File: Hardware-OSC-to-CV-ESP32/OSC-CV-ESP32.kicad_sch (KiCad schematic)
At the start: 10 parts, among them U1 MCP4822, U2 LM324, U3 ESP32-S3-DevKitC, U4 MCP4822

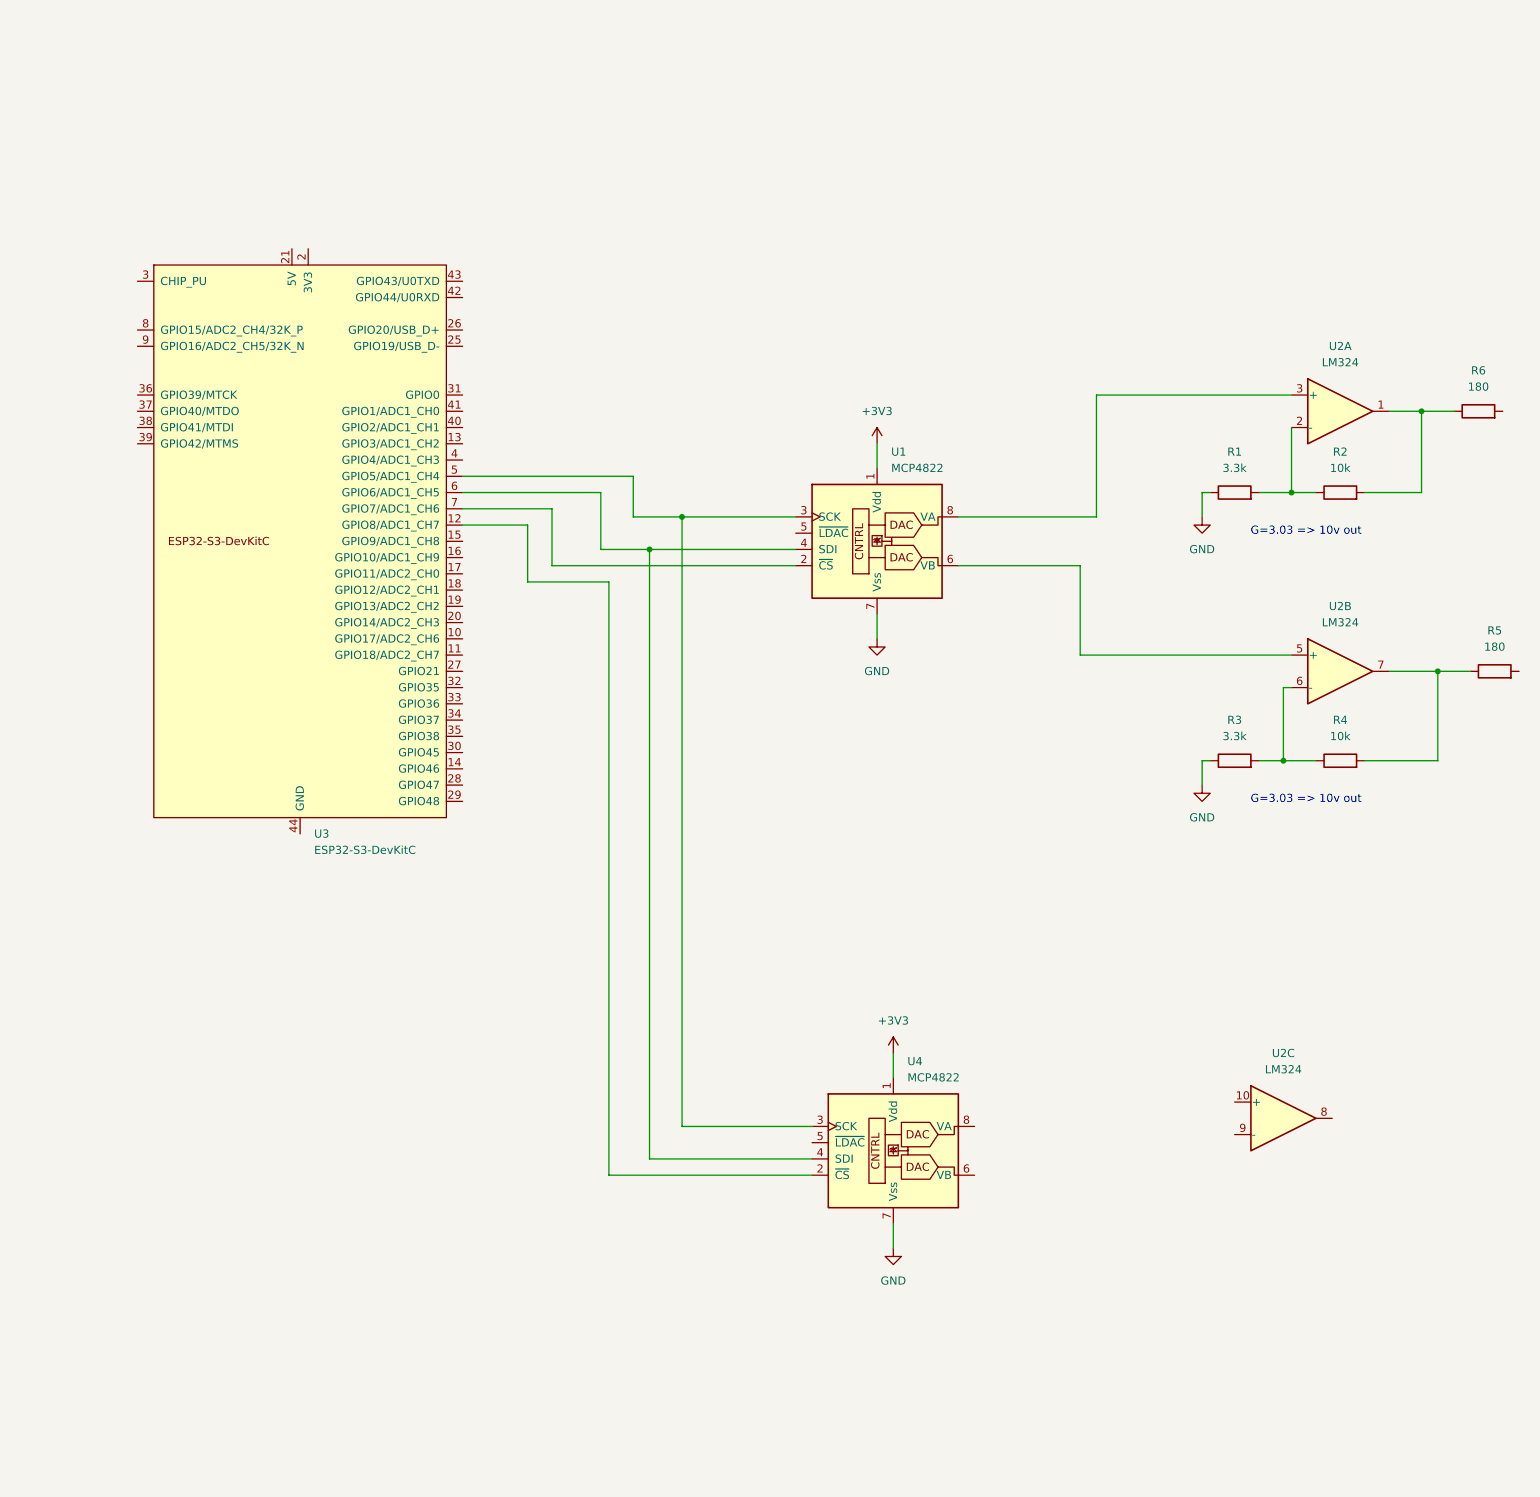
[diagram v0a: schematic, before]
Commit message: update schematic + 3D holder
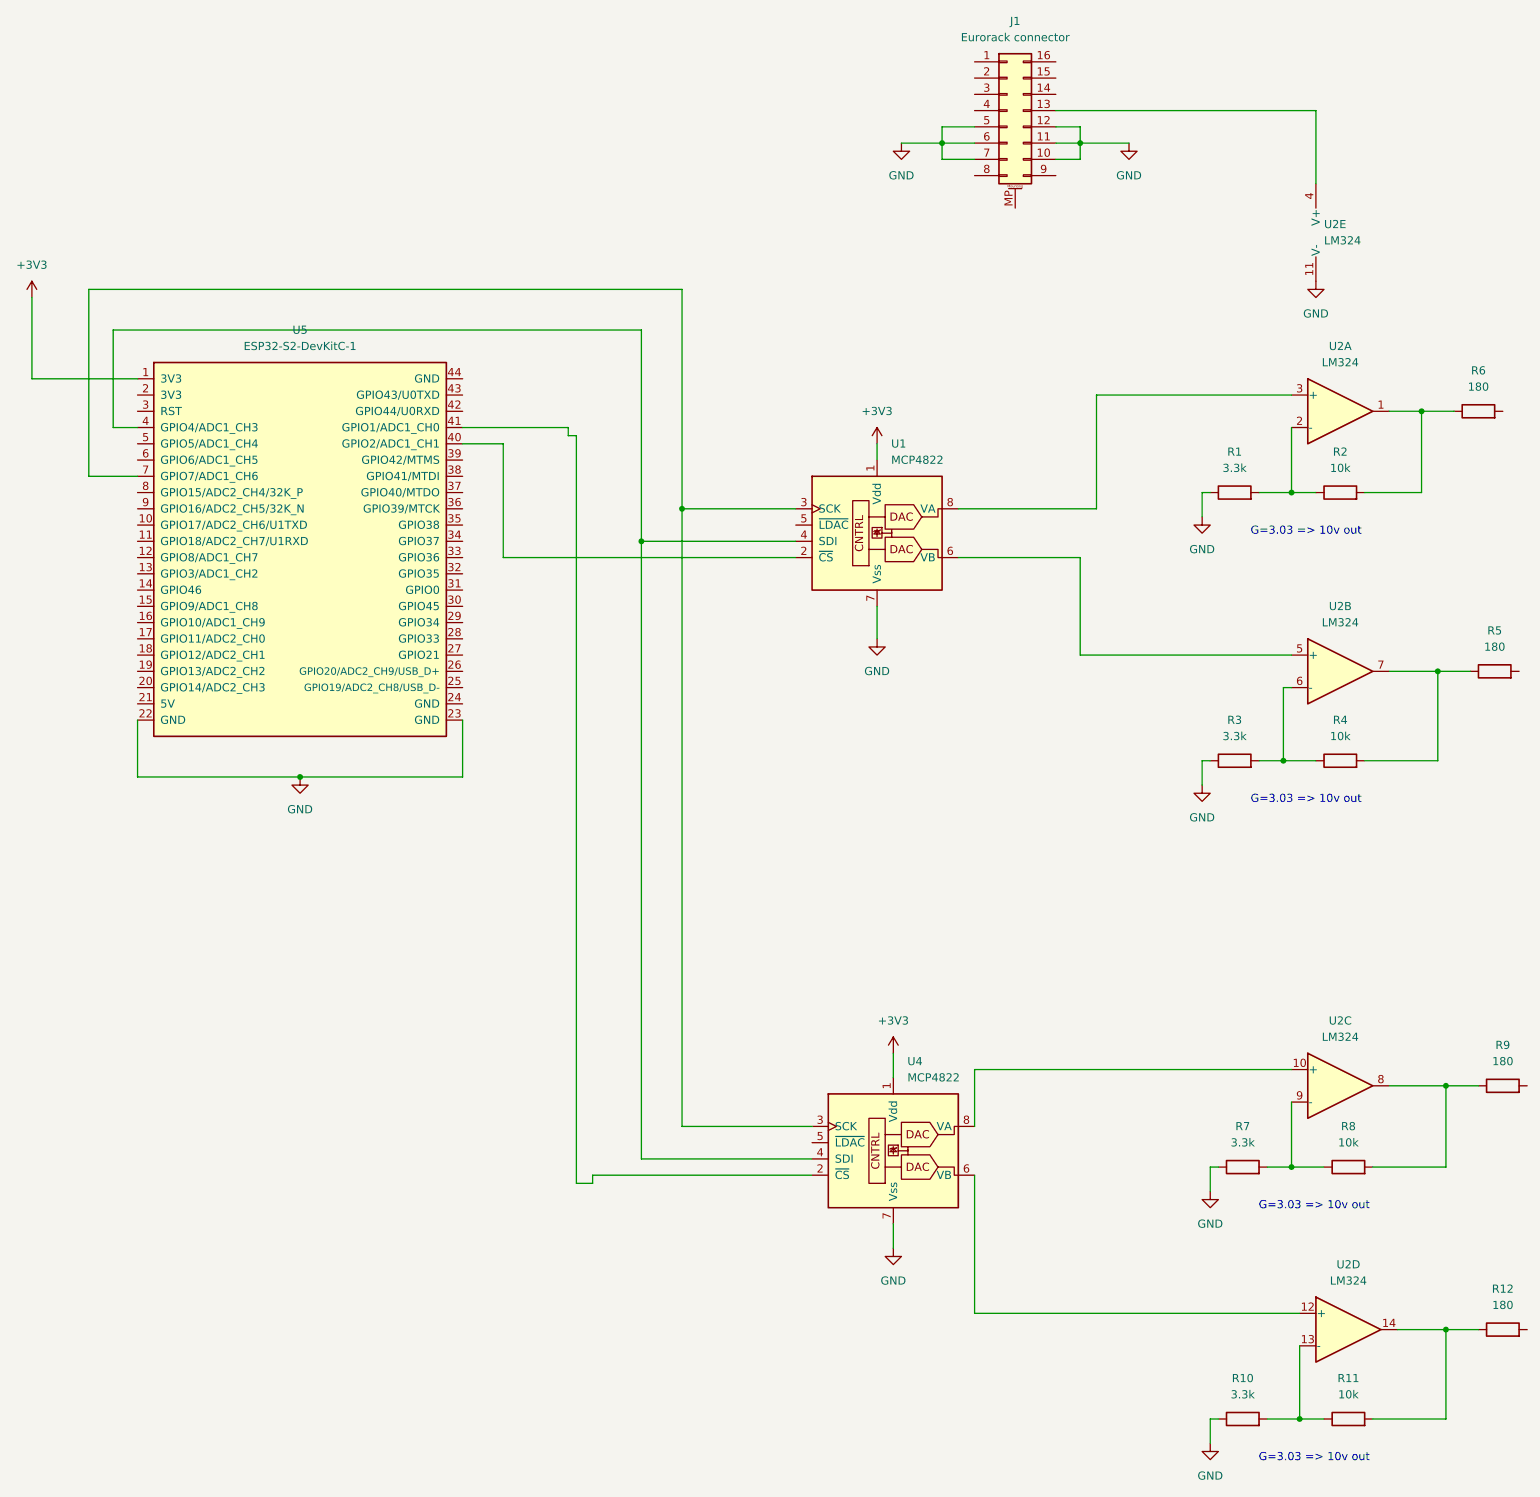
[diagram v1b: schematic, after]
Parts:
- removed U3: ESP32-S3-DevKitC, PCM_Espressif:ESP32-S3-DevKitC, symbol PCM_Espressif:ESP32-S3-DevKitC
- added J1: Eurorack connector, symbol Connector_Generic_MountingPin:Conn_02x08_Counter_Clockwise_MountingPin
- added R10, R7: 3.3k, symbol Device:R
- added R11, R8: 10k, symbol Device:R
- added R12, R9: 180, symbol Device:R
- added unit 4 of U2
- added unit 5 of U2
- added U5: ESP32-S2-DevKitC-1, PCM_Espressif:ESP32-S2-DevKitC-1, symbol PCM_Espressif:ESP32-S2-DevKitC-1
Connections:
- net +3V3: now also U5.1 (3V3)
- net GND: now also J1.10 (Pin_10), J1.11 (Pin_11), J1.12 (Pin_12), J1.5 (Pin_5), J1.6 (Pin_6), J1.7 (Pin_7), R10.1, R7.1, U2.11 (V-), U5.22 (GND), U5.23 (GND)
- net at U2.10 (+): now also U4.8 (VA)
- net at U2.8: now also R8.2, R9.1
- net at U2.9 (-): now also R7.2, R8.1
- net at U1.2 (~{CS}): now also U5.40 (GPIO2/ADC1_CH1)
- net at U1.3 (SCK), U4.3 (SCK): now also U5.7 (GPIO7/ADC1_CH6)
- net at U1.4 (SDI), U4.4 (SDI): now also U5.4 (GPIO4/ADC1_CH3)
- net at U4.2 (~{CS}): now also U5.41 (GPIO1/ADC1_CH0)
- net at U4.6 (VB): now also U2.12 (+)
- new net: R10.2, R11.1, U2.13 (-)
- new net: R11.2, R12.1, U2.14
- new net: J1.13 (Pin_13), U2.4 (V+)
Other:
- moved on the sheet: U1, U2C
